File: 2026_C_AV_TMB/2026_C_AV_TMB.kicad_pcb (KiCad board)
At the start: 2 copper layers, 80 x 80 mm, 34 parts, among them IC1 TLV75533PDYDR, J1 DIN41612_02x16_AB, U1 RFM95W-868S2, U2 RFM95W-868S2, U3 JS4PS-1W+, U4 JS4PS-1W+

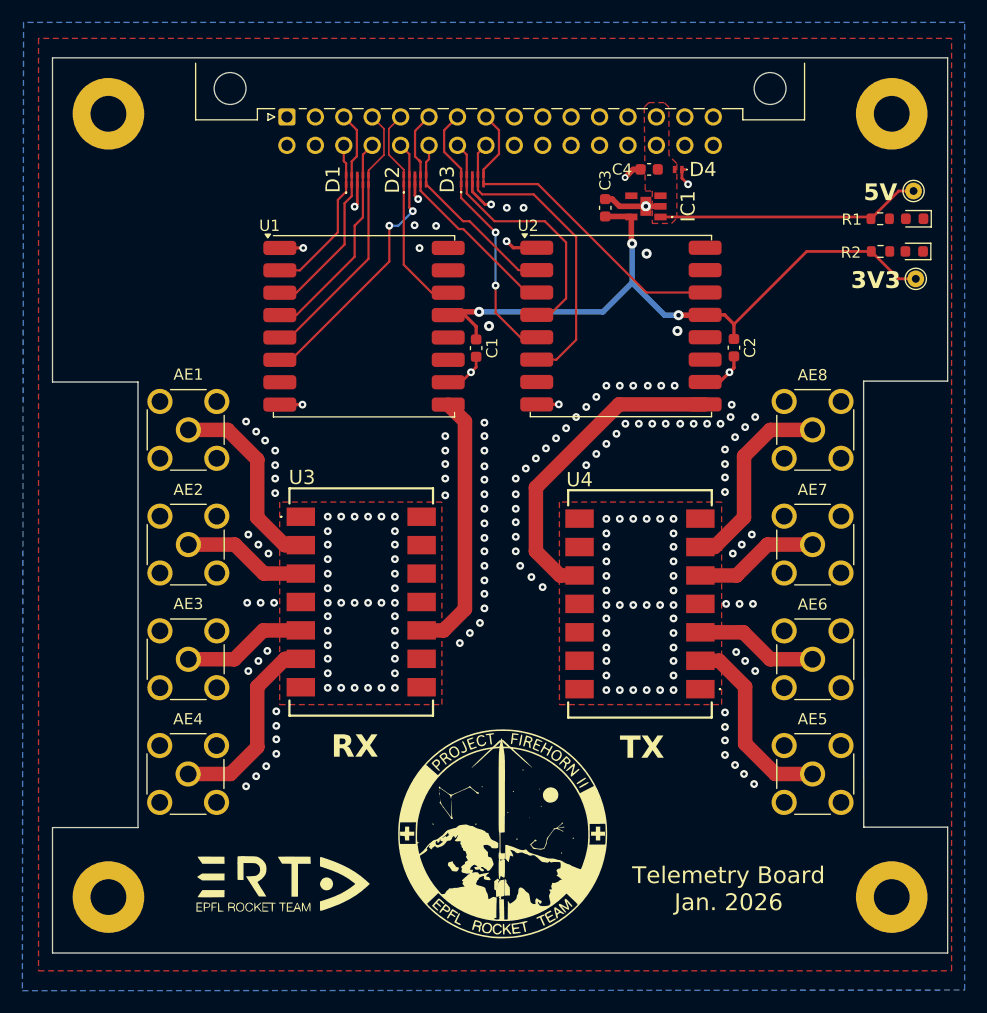
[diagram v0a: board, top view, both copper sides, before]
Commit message: TMB: changed SMA ref
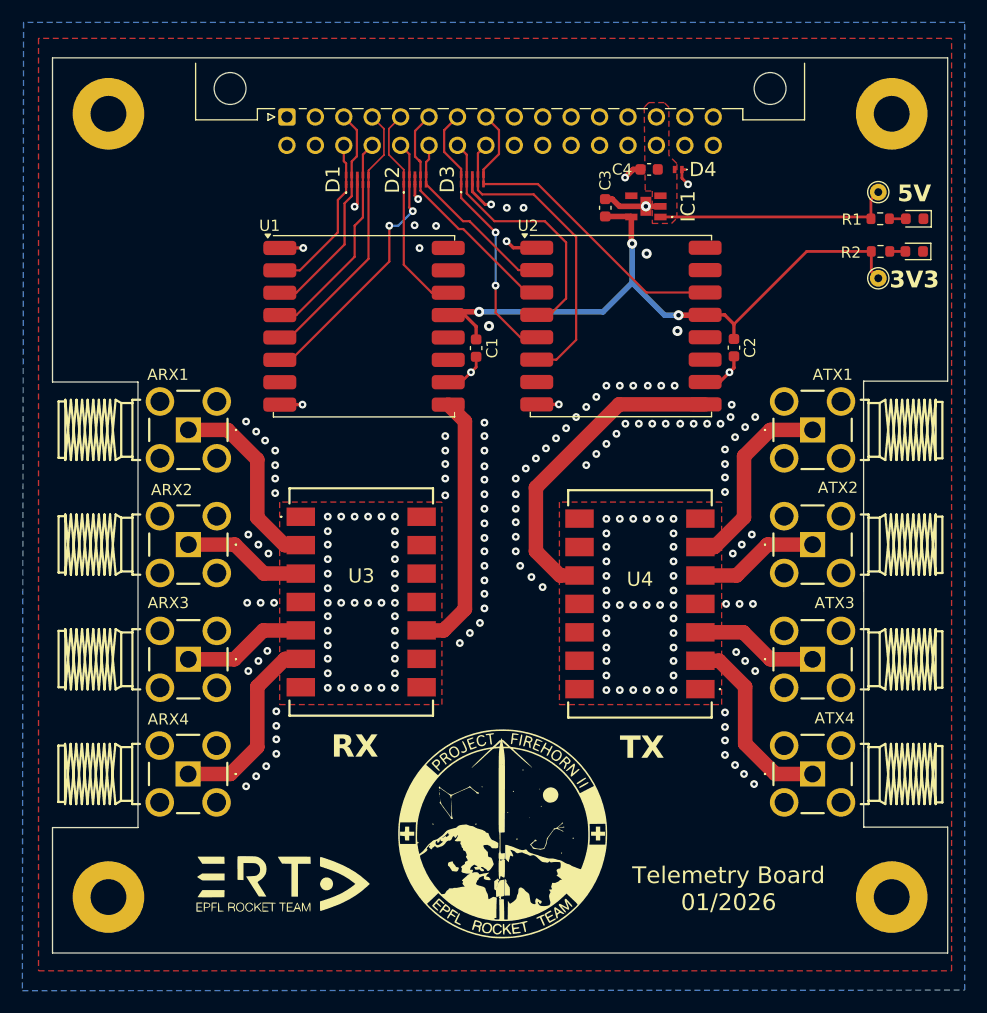
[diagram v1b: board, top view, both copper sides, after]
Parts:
- AE1, AE2, AE3, AE4, AE5, AE6, AE7, AE8: footprint Connector_Coaxial:SMA_Molex_73251-2200_Horizontal -> 901-143-6RFX:9011436RFX
- moved TP2 3.35 mm to (178.8, 79.7)
- moved TP1 3.15 mm to (178.8, 72.0)
- turned AE1 to 180 degrees
- turned AE2 to 180 degrees
- turned AE3 to 180 degrees
- turned AE4 to 180 degrees
- turned AE5 to 0 degrees
- turned AE6 to 0 degrees
- turned AE7 to 0 degrees
- turned AE8 to 0 degrees
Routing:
- net +3V3: track 61.9 -> 59.6 mm
- net +5V: track 23.7 -> 21.5 mm
- net Net-(D5-A): track 0.00 -> 1.47 mm
- net Net-(D6-A): track 0.00 -> 1.40 mm
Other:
- board text added: "ARX1"
- board text added: "ARX2"
- board text added: "ARX3"
- board text added: "ARX4"
- board text added: "ATX1"
- board text added: "ATX2"
- board text added: "ATX3"
- board text added: "ATX4"
- board text added: "Telemetry Board 01/2026"
- board text removed: "Telemetry Board Jan. 2026"
